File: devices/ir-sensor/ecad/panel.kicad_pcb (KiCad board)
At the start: 2 copper layers, 52 x 72 mm, 89 parts, among them J1 SM03B-SRSS-TB, U1 EE-SY1201

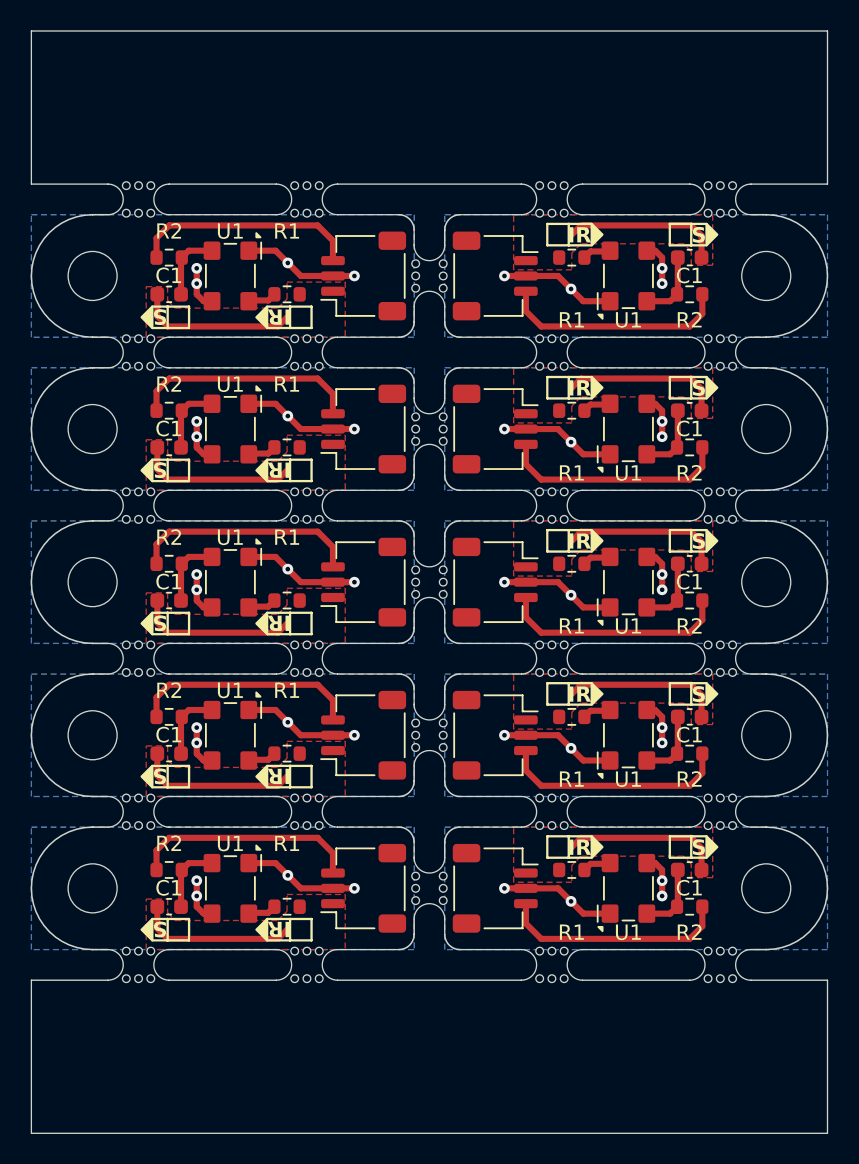
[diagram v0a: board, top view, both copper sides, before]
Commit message: Adds license and output for IR Sensor
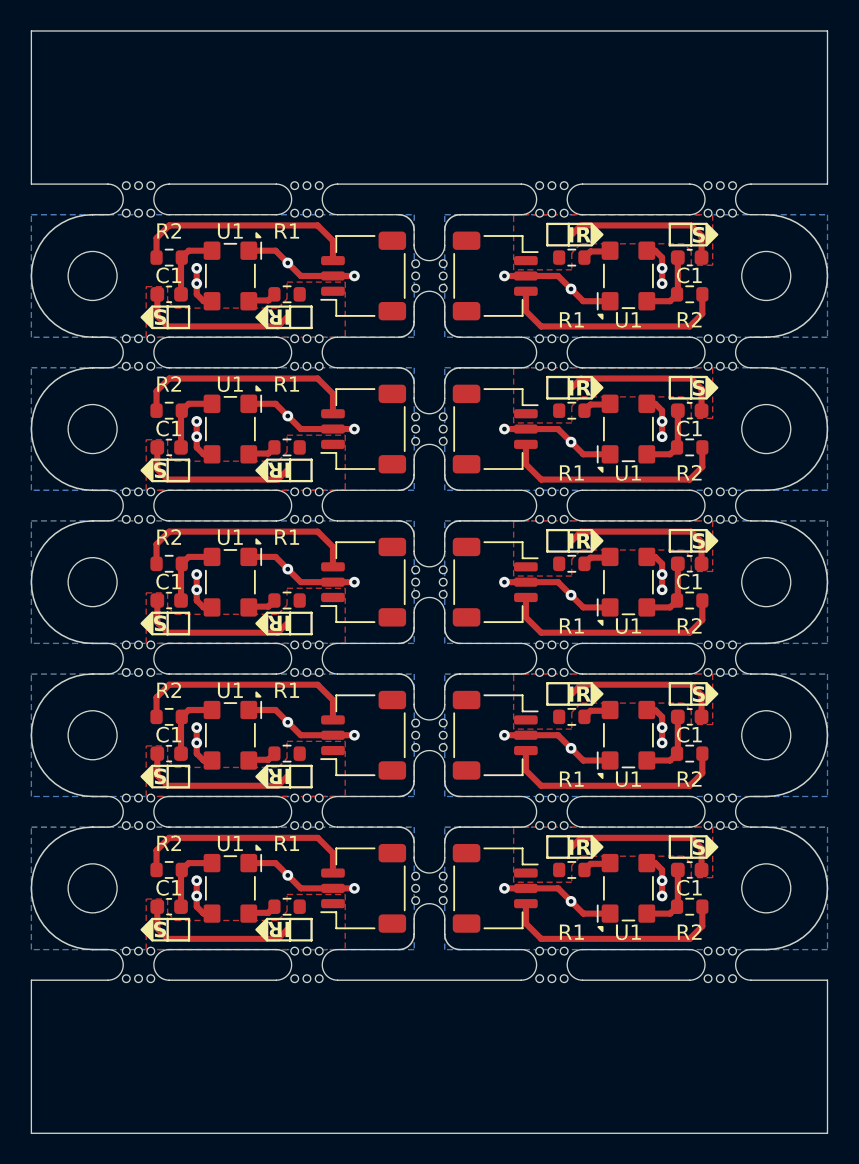
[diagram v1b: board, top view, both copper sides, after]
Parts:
- added REF**: OSHW-Logo_5.7x6mm_SilkScreen, Symbol:OSHW-Logo_5.7x6mm_SilkScreen, B.Cu at (122.0, 93.8)
- added REF**: OSHW-Logo_5.7x6mm_SilkScreen, Symbol:OSHW-Logo_5.7x6mm_SilkScreen, B.Cu at (132.0, 114.2)
- added REF**: OSHW-Logo_5.7x6mm_SilkScreen, Symbol:OSHW-Logo_5.7x6mm_SilkScreen, B.Cu at (132.0, 74.2)
- added REF**: OSHW-Logo_5.7x6mm_SilkScreen, Symbol:OSHW-Logo_5.7x6mm_SilkScreen, B.Cu at (122.0, 83.8)
- added REF**: OSHW-Logo_5.7x6mm_SilkScreen, Symbol:OSHW-Logo_5.7x6mm_SilkScreen, B.Cu at (122.0, 103.8)
- added REF**: OSHW-Logo_5.7x6mm_SilkScreen, Symbol:OSHW-Logo_5.7x6mm_SilkScreen, B.Cu at (122.0, 73.8)
- added REF**: OSHW-Logo_5.7x6mm_SilkScreen, Symbol:OSHW-Logo_5.7x6mm_SilkScreen, B.Cu at (132.0, 84.2)
- added REF**: OSHW-Logo_5.7x6mm_SilkScreen, Symbol:OSHW-Logo_5.7x6mm_SilkScreen, B.Cu at (122.0, 113.8)
- added REF**: OSHW-Logo_5.7x6mm_SilkScreen, Symbol:OSHW-Logo_5.7x6mm_SilkScreen, B.Cu at (132.0, 104.2)
- added REF**: OSHW-Logo_5.7x6mm_SilkScreen, Symbol:OSHW-Logo_5.7x6mm_SilkScreen, B.Cu at (132.0, 94.2)
- turned REF** to 90 degrees (x5)
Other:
- board text added: "IR Sensor Rev A"

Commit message: Corrects PCB for production'
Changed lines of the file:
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@@
 			(size 1.2 1.8)
 			(layers "F.Cu" "F.Paste" "F.Mask")
-			(roundrect_rratio 0.208333)
+			(roundrect_rratio 0.2083333333)
 		)
 		(pad "MP" smd roundrect
@@
 			(size 1.2 1.8)
 			(layers "F.Cu" "F.Paste" "F.Mask")
-			(roundrect_rratio 0.208333)
+			(roundrect_rratio 0.2083333333)
 		)
 		(model "${KIPRJMOD}/../../common/ecad/common.pretty/common.3dshapes/SM03B-SRSS-TB.stp"
@@
 			(size 1.2 1.8)
 			(layers "F.Cu" "F.Paste" "F.Mask")
-			(roundrect_rratio 0.208333)
+			(roundrect_rratio 0.2083333333)
 		)
 		(pad "MP" smd roundrect
@@
 			(size 1.2 1.8)
 			(layers "F.Cu" "F.Paste" "F.Mask")
-			(roundrect_rratio 0.208333)
+			(roundrect_rratio 0.2083333333)
 		)
 		(model "${KIPRJMOD}/../../common/ecad/common.pretty/common.3dshapes/SM03B-SRSS-TB.stp"
@@
 			(size 1.2 1.8)
 			(layers "F.Cu" "F.Paste" "F.Mask")
-			(roundrect_rratio 0.208333)
+			(roundrect_rratio 0.2083333333)
 		)
 		(pad "MP" smd roundrect
@@
 			(size 1.2 1.8)
 			(layers "F.Cu" "F.Paste" "F.Mask")
-			(roundrect_rratio 0.208333)
+			(roundrect_rratio 0.2083333333)
 		)
 		(model "${KIPRJMOD}/../../common/ecad/common.pretty/common.3dshapes/SM03B-SRSS-TB.stp"
@@
 			(size 1.2 1.8)
 			(layers "F.Cu" "F.Paste" "F.Mask")
-			(roundrect_rratio 0.208333)
+			(roundrect_rratio 0.2083333333)
 		)
 		(pad "MP" smd roundrect
@@
 			(size 1.2 1.8)
 			(layers "F.Cu" "F.Paste" "F.Mask")
-			(roundrect_rratio 0.208333)
+			(roundrect_rratio 0.2083333333)
 		)
 		(model "${KIPRJMOD}/../../common/ecad/common.pretty/common.3dshapes/SM03B-SRSS-TB.stp"
@@
 			(size 1.2 1.8)
 			(layers "F.Cu" "F.Paste" "F.Mask")
-			(roundrect_rratio 0.208333)
+			(roundrect_rratio 0.2083333333)
 		)
 		(pad "MP" smd roundrect
@@
 			(size 1.2 1.8)
 			(layers "F.Cu" "F.Paste" "F.Mask")
-			(roundrect_rratio 0.208333)
+			(roundrect_rratio 0.2083333333)
 		)
 		(model "${KIPRJMOD}/../../common/ecad/common.pretty/common.3dshapes/SM03B-SRSS-TB.stp"
@@
 			(size 1.2 1.8)
 			(layers "F.Cu" "F.Paste" "F.Mask")
-			(roundrect_rratio 0.208333)
+			(roundrect_rratio 0.2083333333)
 		)
 		(pad "MP" smd roundrect
@@
 			(size 1.2 1.8)
 			(layers "F.Cu" "F.Paste" "F.Mask")
-			(roundrect_rratio 0.208333)
+			(roundrect_rratio 0.2083333333)
 		)
 		(model "${KIPRJMOD}/../../common/ecad/common.pretty/common.3dshapes/SM03B-SRSS-TB.stp"
@@
 			(size 1.2 1.8)
 			(layers "F.Cu" "F.Paste" "F.Mask")
-			(roundrect_rratio 0.208333)
+			(roundrect_rratio 0.2083333333)
 		)
 		(pad "MP" smd roundrect
@@
 			(size 1.2 1.8)
 			(layers "F.Cu" "F.Paste" "F.Mask")
-			(roundrect_rratio 0.208333)
+			(roundrect_rratio 0.2083333333)
 		)
 		(model "${KIPRJMOD}/../../common/ecad/common.pretty/common.3dshapes/SM03B-SRSS-TB.stp"
@@
 			(size 1.2 1.8)
 			(layers "F.Cu" "F.Paste" "F.Mask")
-			(roundrect_rratio 0.208333)
+			(roundrect_rratio 0.2083333333)
 		)
 		(pad "MP" smd roundrect
@@
 			(size 1.2 1.8)
 			(layers "F.Cu" "F.Paste" "F.Mask")
-			(roundrect_rratio 0.208333)
+			(roundrect_rratio 0.2083333333)
 		)
 		(model "${KIPRJMOD}/../../common/ecad/common.pretty/common.3dshapes/SM03B-SRSS-TB.stp"
@@
 			(size 1.2 1.8)
 			(layers "F.Cu" "F.Paste" "F.Mask")
-			(roundrect_rratio 0.208333)
+			(roundrect_rratio 0.2083333333)
 		)
 		(pad "MP" smd roundrect
@@
 			(size 1.2 1.8)
 			(layers "F.Cu" "F.Paste" "F.Mask")
-			(roundrect_rratio 0.208333)
+			(roundrect_rratio 0.2083333333)
 		)
 		(model "${KIPRJMOD}/../../common/ecad/common.pretty/common.3dshapes/SM03B-SRSS-TB.stp"
@@
 			(size 1.2 1.8)
 			(layers "F.Cu" "F.Paste" "F.Mask")
-			(roundrect_rratio 0.208333)
+			(roundrect_rratio 0.2083333333)
 		)
 		(pad "MP" smd roundrect
@@
 			(size 1.2 1.8)
 			(layers "F.Cu" "F.Paste" "F.Mask")
-			(roundrect_rratio 0.208333)
+			(roundrect_rratio 0.2083333333)
 		)
 		(model "${KIPRJMOD}/../../common/ecad/common.pretty/common.3dshapes/SM03B-SRSS-TB.stp"
